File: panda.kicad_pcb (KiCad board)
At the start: 2 copper layers, 144.8 x 38.1 mm, 33 parts, among them J1 USB, J2 ICSP, U1 ATMEGA8, U2 MAX7219, Y1 16MHz

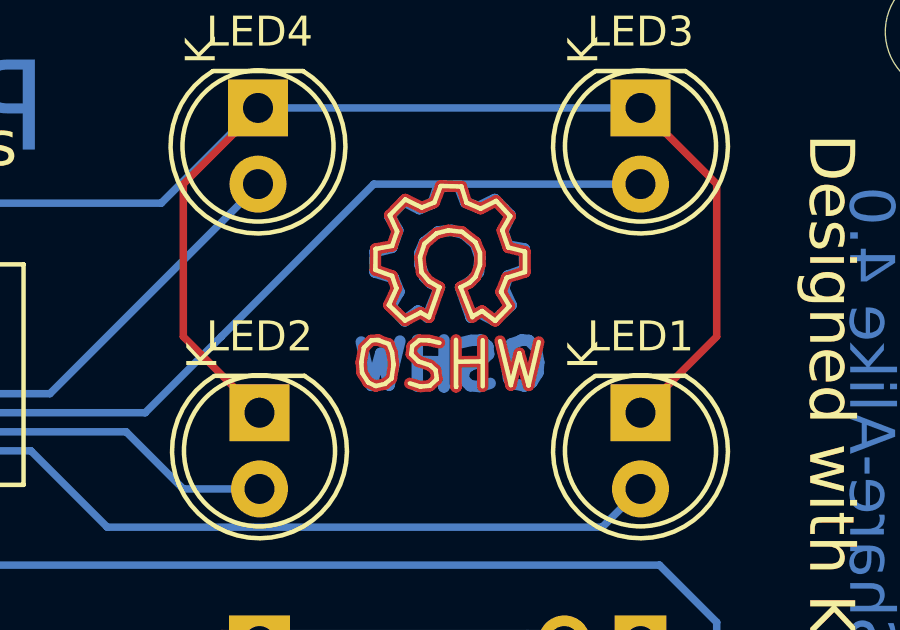
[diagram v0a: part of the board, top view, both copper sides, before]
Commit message: Shift OSH logo down to avoid hitting the LED3's column trace.
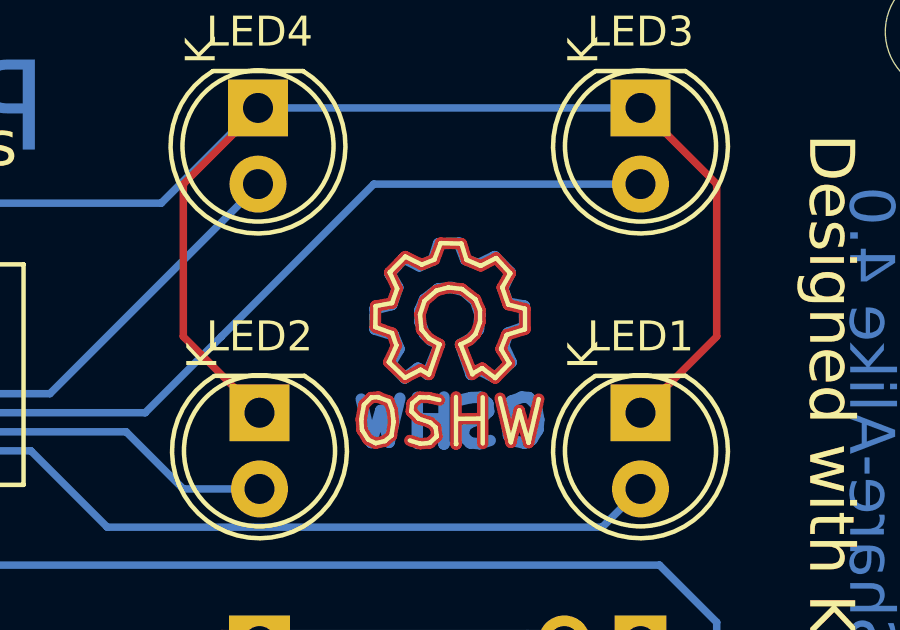
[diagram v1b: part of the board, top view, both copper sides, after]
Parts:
- moved REF** 1.91 mm to (181.6, 98.4) (x4)
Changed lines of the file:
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@@
     (links 130)
     (no_connects 0)
-    (area 55.804999 86.284999 200.735001 124.535001)
+    (area 43.742352 80.79 217.674286 132.222038)
     (thickness 1.6)
     (drawings 27)
@@
   )
   (module Symbols:Symbol_OSHW-Logo_CopperTop (layer B.Cu)
-    (at 181.61 96.52 180)
+    (at 181.61 98.425 180)
     (descr "Symbol, OSHW-Logo, Copper Top,")
     (tags "Symbol, OSHW-Logo, Copper Top,")
@@
   )
   (module Symbols:Symbol_OSHW-Logo_CopperTop (layer F.Cu)
-    (at 181.61 96.52)
+    (at 181.61 98.425)
     (descr "Symbol, OSHW-Logo, Copper Top,")
     (tags "Symbol, OSHW-Logo, Copper Top,")
@@
   )
   (module Symbols:Symbol_OSHW-Logo_SilkScreen (layer F.Cu)
-    (at 181.61 96.52)
+    (at 181.61 98.425)
     (descr "Symbol, OSHW-Logo, Silk Screen,")
     (tags "Symbol, OSHW-Logo, Silk Screen,")
@@
   )
   (module Symbols:Symbol_OSHW-Logo_SilkScreen (layer B.Cu)
-    (at 181.61 96.52 180)
+    (at 181.61 98.425 180)
     (descr "Symbol, OSHW-Logo, Silk Screen,")
     (tags "Symbol, OSHW-Logo, Silk Screen,")

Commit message: Clean up lots of messiness.
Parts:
- removed the REF** at (181.6, 98.4) (x4)
- added REF***: OSHW-Logo_7.5x8mm_SilkScreen, Symbols:OSHW-Logo_7.5x8mm_SilkScreen, B.Cu at (60.3, 100.3)
- added REF***: KiCad-Logo2_6mm_SilkScreen, Symbols:KiCad-Logo2_6mm_SilkScreen, B.Cu at (184.2, 120.7)
- added REF***: OSHW-Logo_7.5x8mm_Copper, Symbols:OSHW-Logo_7.5x8mm_Copper, B.Cu at (181.6, 99.1)
- added REF***: OSHW-Logo_7.5x8mm_Copper, Symbols:OSHW-Logo_7.5x8mm_Copper, F.Cu at (181.6, 97.8)
- added REF***: KiCad-Logo2_6mm_SilkScreen, Symbols:KiCad-Logo2_6mm_SilkScreen, F.Cu at (183.5, 120.7)
- added REF***: OSHW-Logo_7.5x8mm_SilkScreen, Symbols:OSHW-Logo_7.5x8mm_SilkScreen, F.Cu at (60.3, 111.8)
- C1: value 10uF -> 4.7uF; footprint Capacitors_ThroughHole:C_Radial_D5_L6_P2.5 -> Capacitors_THT:CP_Radial_D5.0mm_P2.50mm; moved to F.Cu
- C2, C3, C4, C5: footprint Capacitors_ThroughHole:C_Rect_L4_W2.5_P2.5 -> Capacitors_THT:C_Disc_D3.0mm_W1.6mm_P2.50mm
- D1, D2: footprint Diodes_ThroughHole:Diode_DO-35_SOD27_Horizontal_RM10 -> Diodes_THT:D_DO-35_SOD27_P7.62mm_Horizontal
- J1: footprint Pin_Headers:Pin_Header_Straight_1x04 -> Pin_Headers:Pin_Header_Straight_1x04_Pitch2.54mm
- J2: footprint Pin_Headers:Pin_Header_Straight_2x03 -> Pin_Headers:Pin_Header_Straight_2x03_Pitch2.54mm
- LED1, LED2, LED3, LED4: footprint LEDs:LED-5MM -> LEDs:LED_D5.0mm
- R1, R2, R3, R4, R5: footprint My_Resistors_ThroughHole:Resistor_Horizontal_RM7.62mm -> Resistors_THT:R_Axial_DIN0204_L3.6mm_D1.6mm_P7.62mm_Horizontal
- moved C2 43.2 mm to (121.9, 114.3)
- moved C3 40.7 mm to (78.7, 111.8), turned to 270 degrees
- moved C5 2.54 mm to (142.2, 111.8)
- moved C4 2.54 mm to (127.0, 111.8)
- moved C1 2.50 mm to (165.1, 116.8)
- moved Y1 0.30 mm to (132.3, 113.0)
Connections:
- C2 pad 1: VCC -> GND
- C2 pad 2: GND -> VCC
- C3 pad 1: VCC -> GND
- C3 pad 2: GND -> VCC
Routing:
- net VCC: track 130.8 -> 137.3 mm, vias 1 -> 2
- net GND: track 141.4 -> 138.4 mm
- net Net-(C5-Pad2): track 10.6 -> 12.2 mm
- net Net-(C4-Pad2): track 9.42 -> 10.8 mm
- net /D+: track 25.6 -> 25.0 mm
- net COL3: track 139.9 -> 140.4 mm
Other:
- board text removed: "Designed with KiCad EDA"

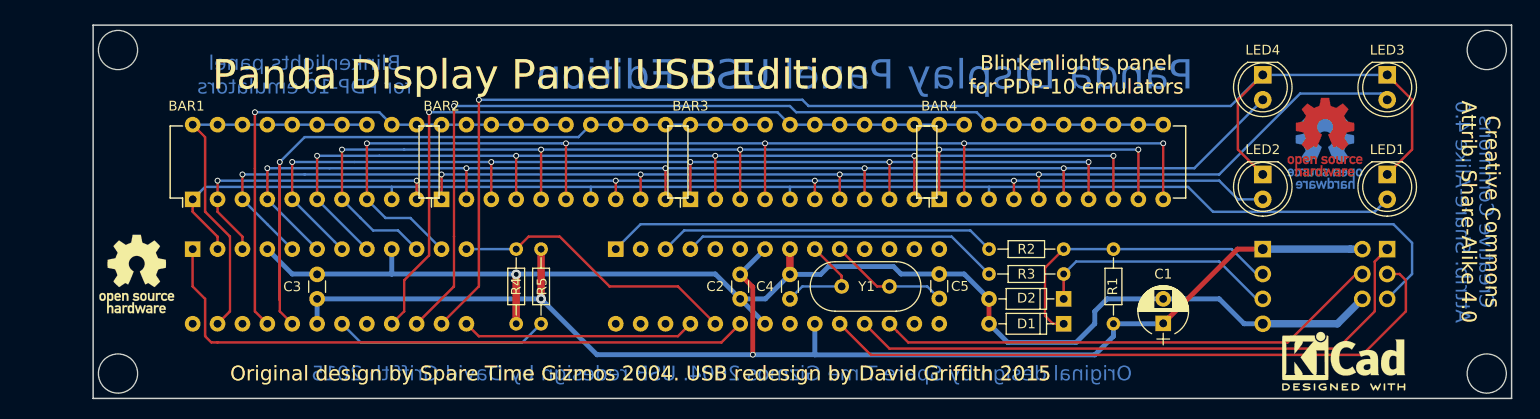
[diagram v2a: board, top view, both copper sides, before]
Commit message: Moved around silks.  Added helpful legends.
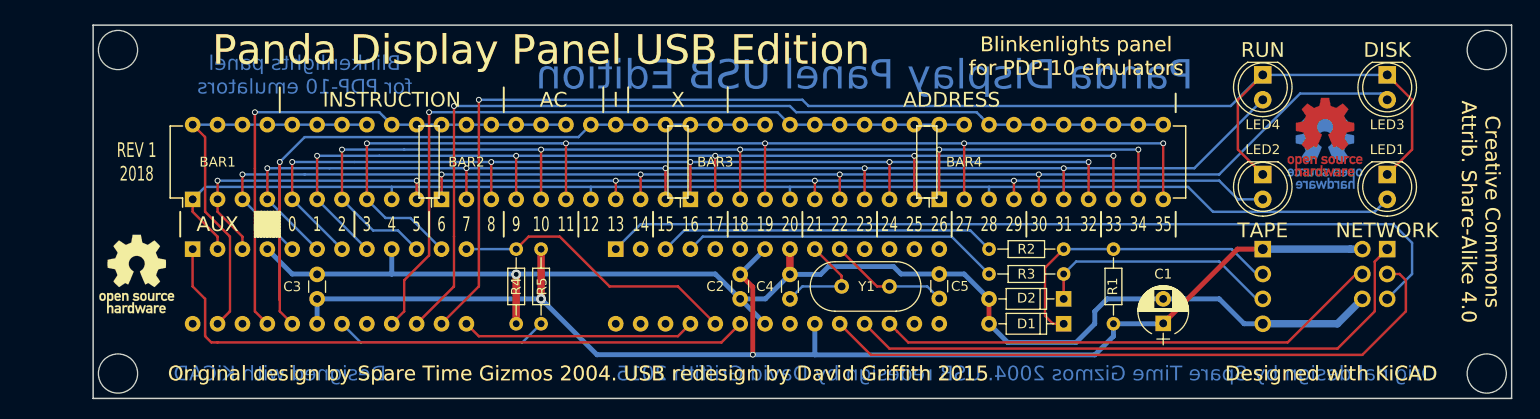
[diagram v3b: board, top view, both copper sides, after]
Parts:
- removed the REF*** at (184.2, 120.7)
- removed the REF*** at (183.5, 120.7)
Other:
- board text added: "0"
- board text added: "1"
- board text added: "10"
- board text added: "11"
- board text added: "12"
- board text added: "13"
- board text added: "14"
- board text added: "15"
- board text added: "16"
- board text added: "17"
- board text added: "18"
- board text added: "19"
- board text added: "2"
- board text added: "20"
- board text added: "21"
- board text added: "22"
- board text added: "23"
- board text added: "24"
- board text added: "25"
- board text added: "26"
- board text added: "27"
- board text added: "28"
- board text added: "29"
- board text added: "3"
- board text added: "30"
- board text added: "31"
- board text added: "32"
- board text added: "33"
- board text added: "34"
- board text added: "35"
- board text added: "4"
- board text added: "5"
- board text added: "6"
- board text added: "7"
- board text added: "8"
- board text added: "9"
- board text added: "AC"
- board text added: "ADDRESS"
- board text added: "AUX"
- board text added: "DISK"
- board text added: "Designed with KiCAD"
- board text added: "I"
- board text added: "INSTRUCTION"
- board text added: "NETWORK"
- board text added: "REV 1 2018"
- board text added: "RUN"
- board text added: "TAPE"
- board text added: "X"

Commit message: Scoot chips down a bit to make room for nicer looking Program Data legends.
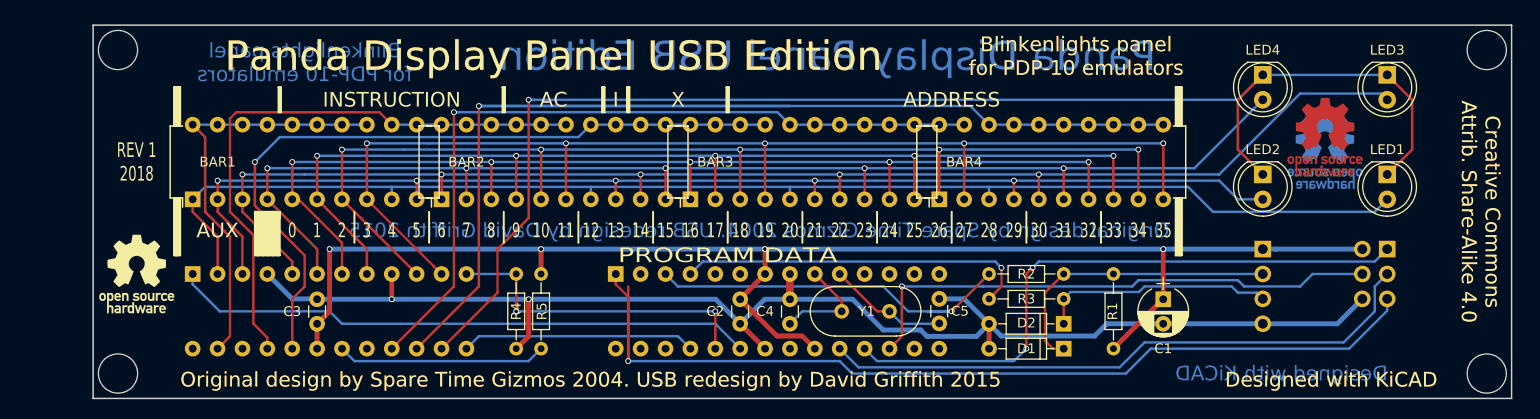
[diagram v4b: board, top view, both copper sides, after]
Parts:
- moved C2 2.54 mm to (121.9, 116.8)
- moved C3 2.54 mm to (78.7, 114.3)
- moved C4 2.54 mm to (127.0, 114.3)
- moved D1 2.54 mm to (154.9, 119.4)
- moved D2 2.54 mm to (154.9, 116.8)
- moved R1 2.54 mm to (160.0, 111.8)
- moved R2 2.54 mm to (154.9, 111.8)
- moved R3 2.54 mm to (154.9, 114.3)
- moved R4 2.54 mm to (99.1, 111.8)
- moved U1 2.54 mm to (109.2, 111.8)
- moved U2 2.54 mm to (66.0, 111.8)
- moved C5 2.54 mm to (142.2, 114.3)
- moved R5 2.54 mm to (101.6, 119.4)
- moved Y1 2.54 mm to (132.3, 115.6)
- moved C1 2.46 mm to (165.1, 114.3), turned to 270 degrees
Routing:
- net ROW5: track 97.0 -> 129.8 mm
- net VCC: track 137.3 -> 147.6 mm, vias 2 -> 4
- net /RESET: track 89.9 -> 98.9 mm, vias 0 -> 1
- net ROW3: track 82.3 -> 75.3 mm
- net ROW2: track 54.4 -> 60.2 mm, vias 1 -> 0
- net /DIN: track 65.1 -> 59.7 mm
- net /SCK: track 66.3 -> 62.1 mm
- net Net-(R2-Pad2): track 34.6 -> 38.7 mm, vias 0 -> 1
- net GND: track 138.4 -> 142.1 mm, vias 1 -> 2
- net Net-(R3-Pad2): track 32.6 -> 36.2 mm, vias 0 -> 1
- net /MOSI: track 51.9 -> 55.6 mm, vias 0 -> 1
- net /LOAD: track 29.6 -> 33.0 mm, vias 0 -> 2
- net COL5: track 107.5 -> 110.4 mm
- net COL3: track 140.4 -> 142.9 mm
- net COL1: track 135.2 -> 137.8 mm
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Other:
- board text added: "PROGRAM DATA"
- board text removed: "DISK"
- board text removed: "NETWORK"
- board text removed: "RUN"
- board text removed: "TAPE"
